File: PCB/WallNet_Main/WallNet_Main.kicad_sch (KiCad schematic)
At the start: 9 parts, among them J1 Conn_01x05_Pin, SW1 SW, U1 BT832

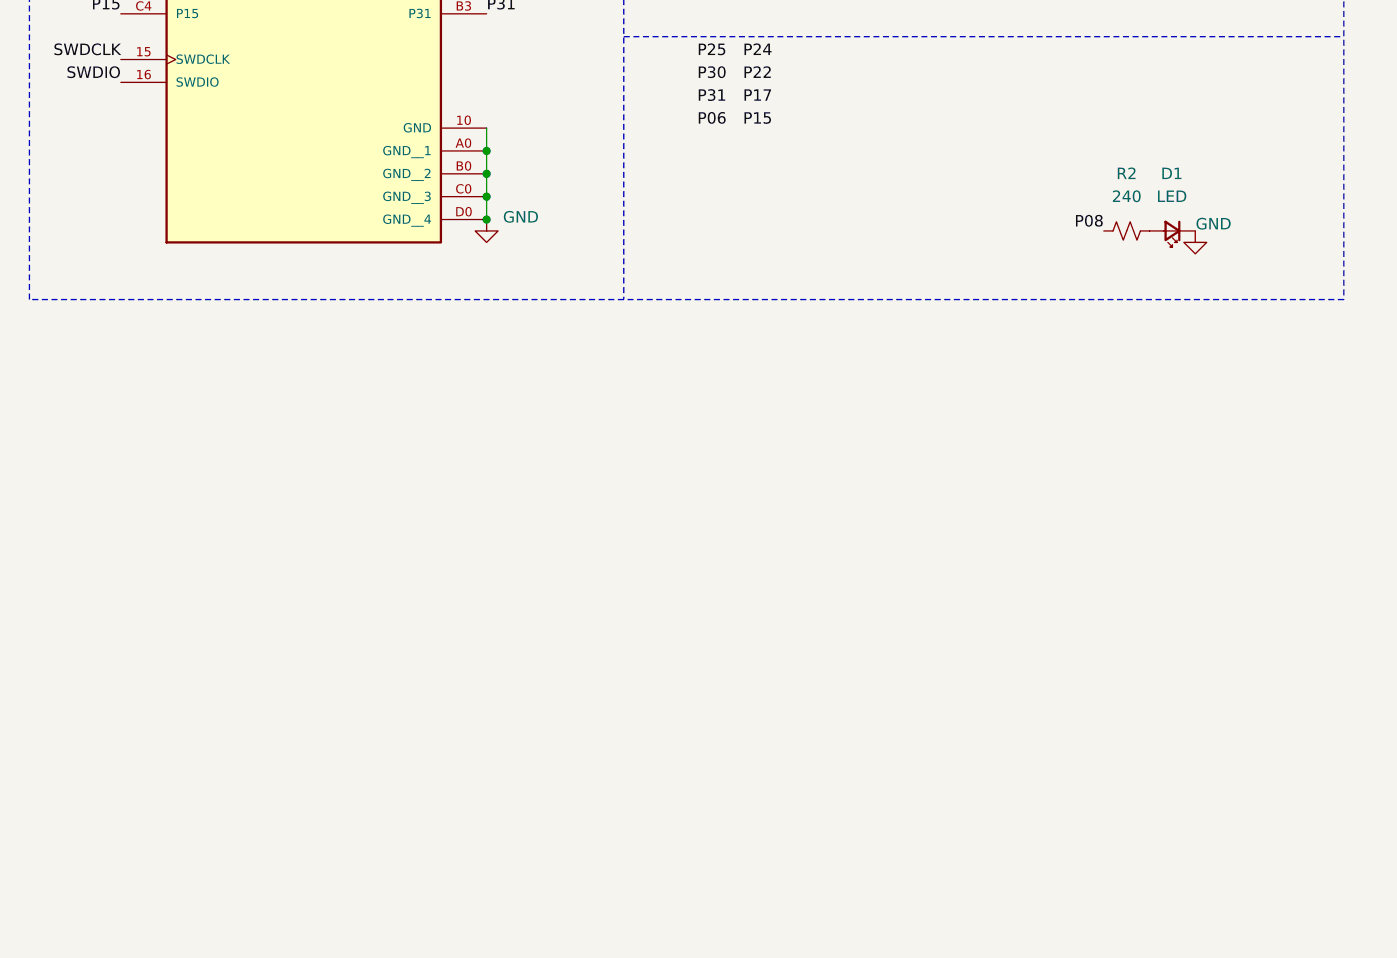
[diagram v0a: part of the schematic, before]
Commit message: "added test point debugging and mounting holes"
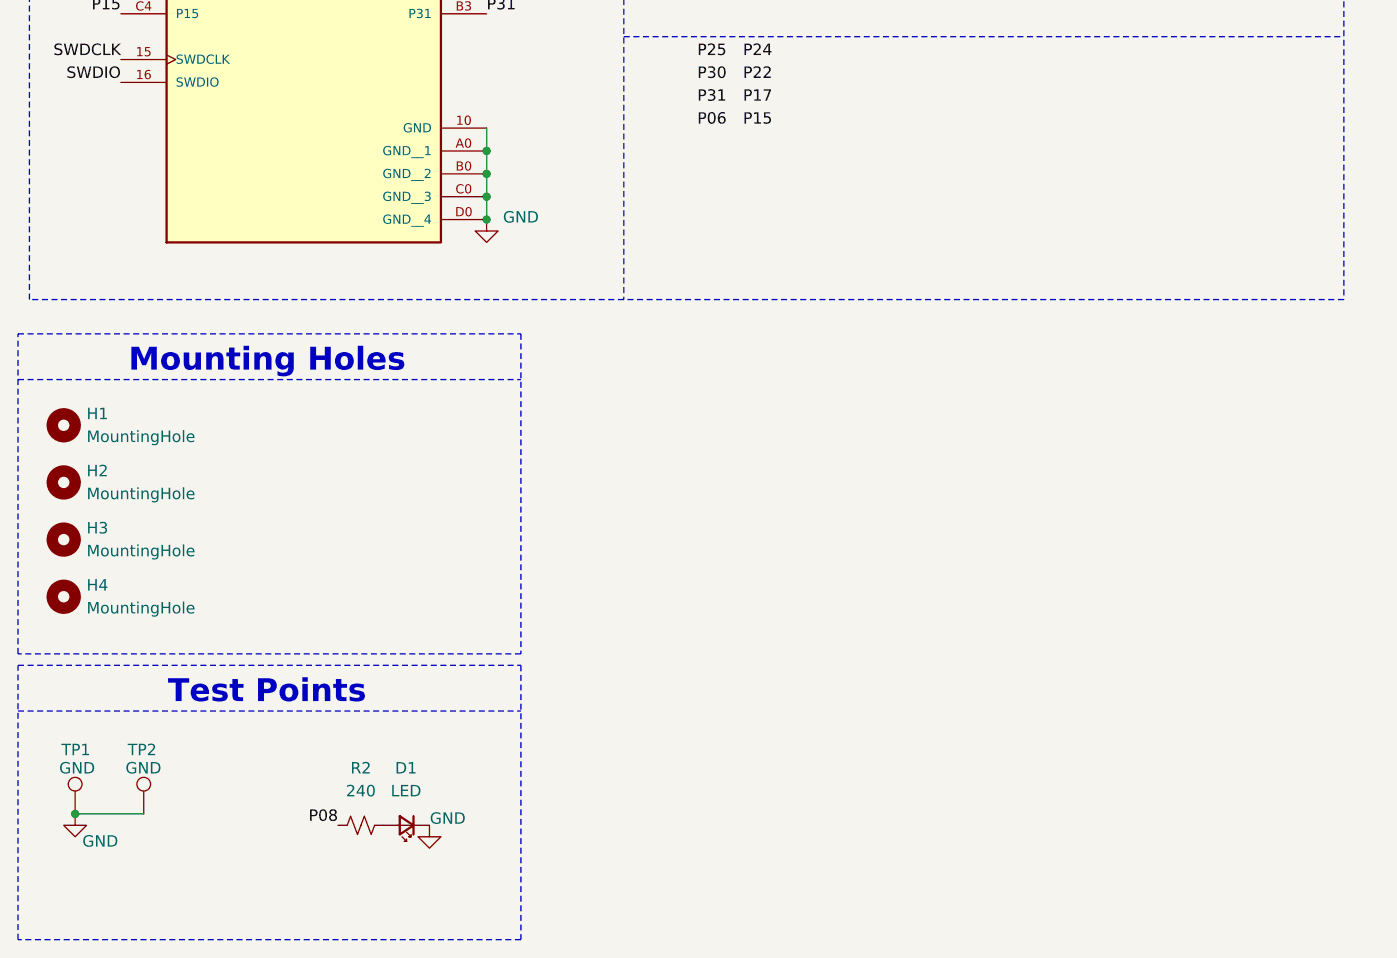
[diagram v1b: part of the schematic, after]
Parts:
- added H1, H2, H3, H4: MountingHole, MountingHole:MountingHole_4.3mm_M4, symbol Mechanical:MountingHole
- added TP1: GND, TestPoint:TestPoint_Pad_D1.0mm, symbol Connector:TestPoint
- added TP2: GND, 5001:KEYSTONE_5001, symbol Connector:TestPoint
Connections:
- net GND: now also TP1.1, TP2.1
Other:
- note added: "Mounting Holes"
- note added: "Test Points"
- moved on the sheet: D1, R2

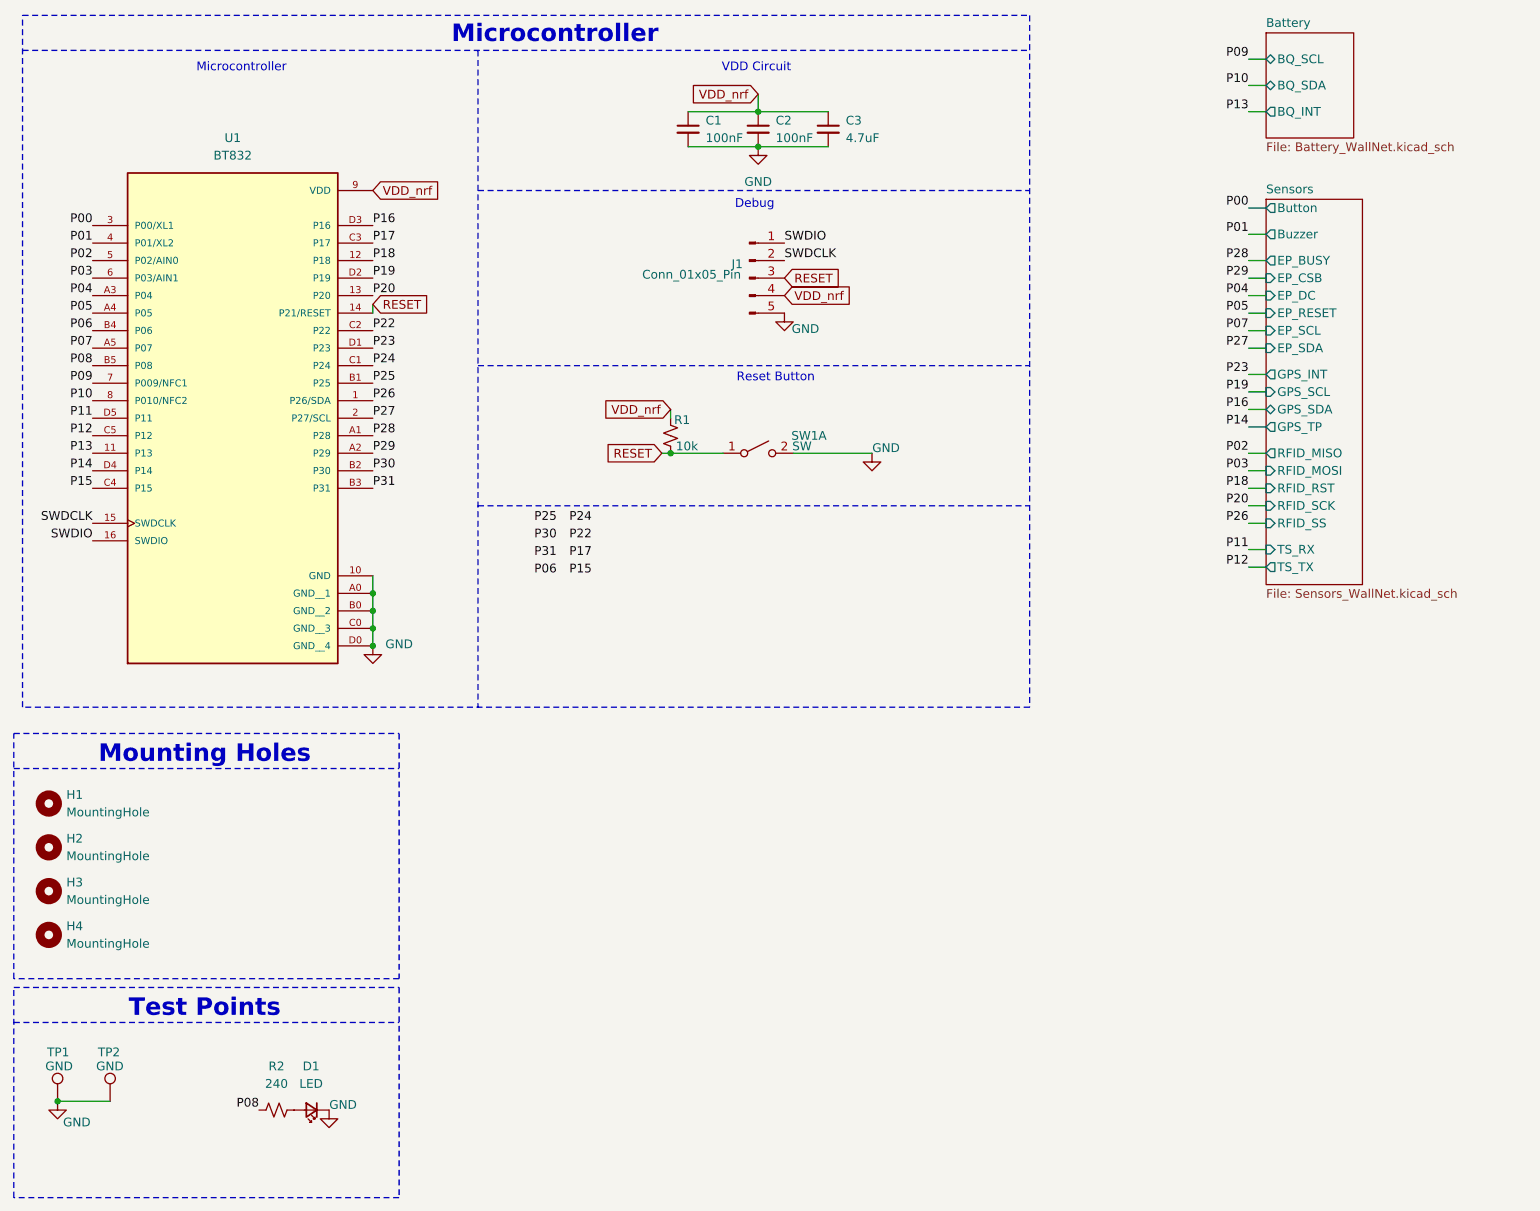
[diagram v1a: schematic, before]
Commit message: Finished adding cutout, via, and mount hole for RFID
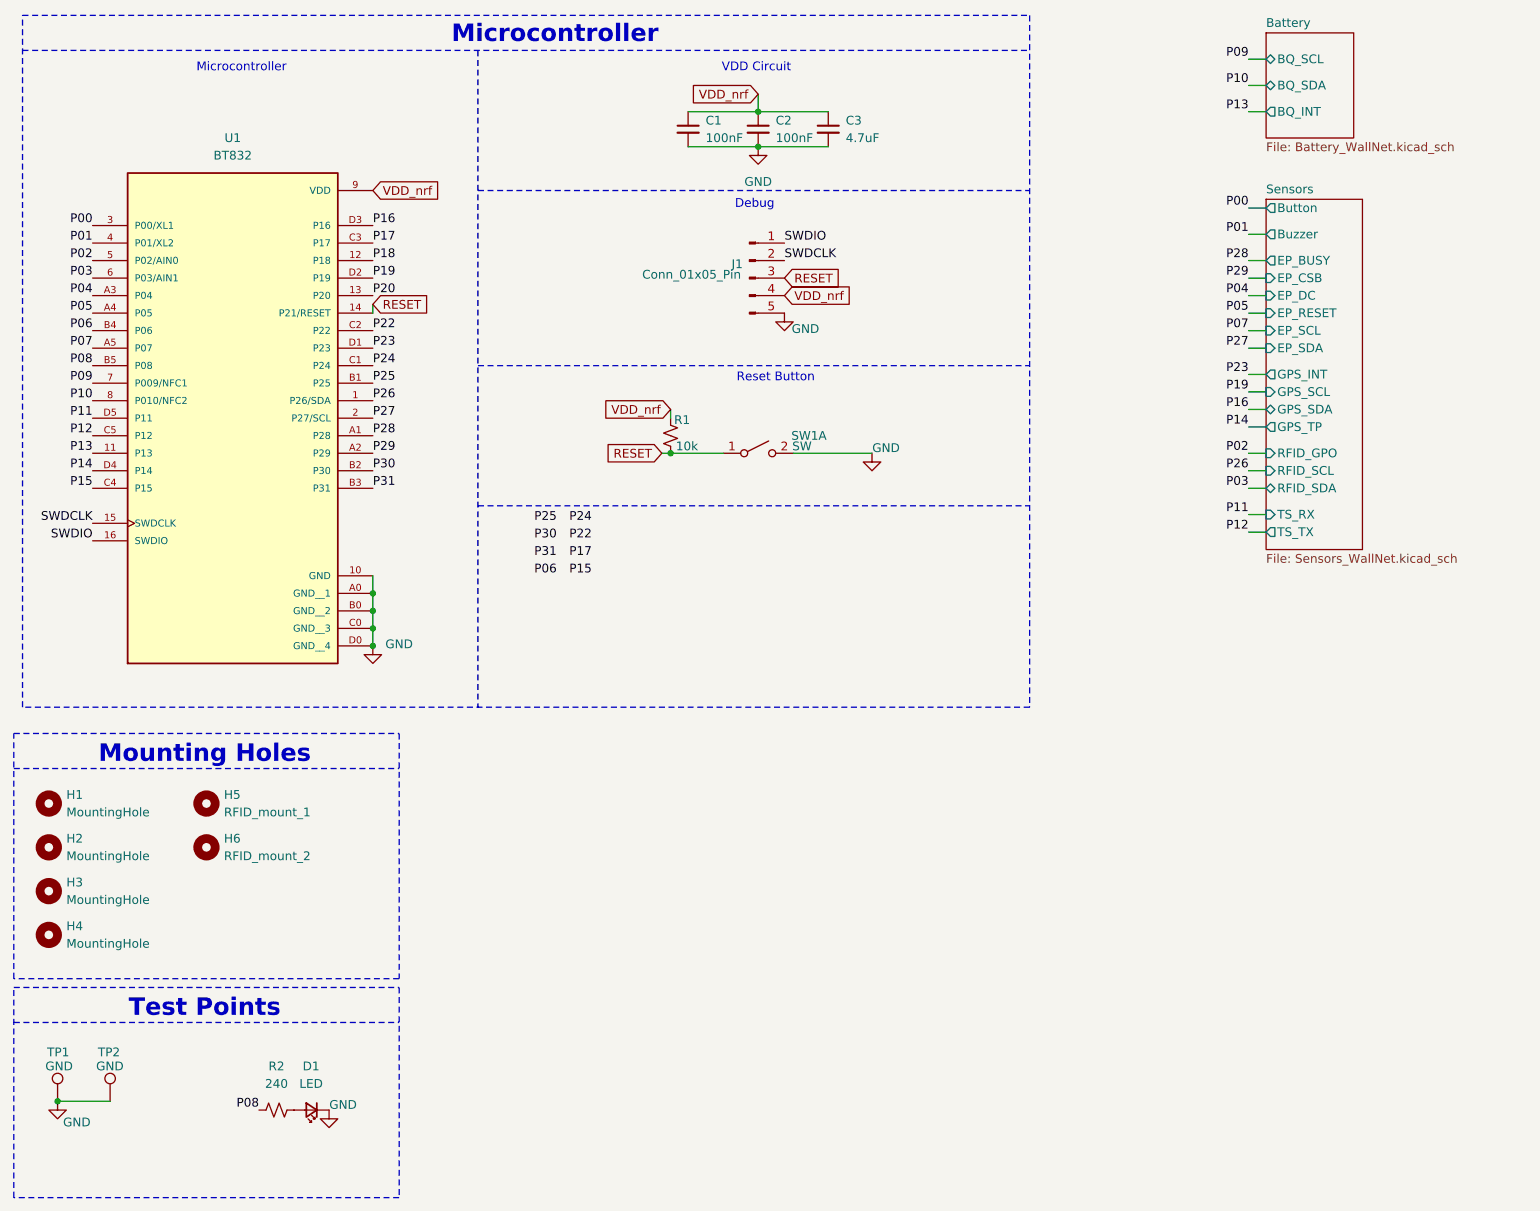
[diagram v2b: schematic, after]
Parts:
- added H5: RFID_mount_1, MountingHole:MountingHole_4.3mm_M4, symbol Mechanical:MountingHole
- added H6: RFID_mount_2, MountingHole:MountingHole_4.3mm_M4, symbol Mechanical:MountingHole
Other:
- sheet Sensors ports: added RFID_GPO, RFID_SCL, RFID_SDA; removed RFID_MISO, RFID_MOSI, RFID_RST, RFID_SCK, RFID_SS
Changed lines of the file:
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@@
 	(wire
 		(pts
-			(xy 68.58 64.77) (xy 68.58 66.04)
+			(xy 195.58 91.44) (xy 198.12 91.44)
 		)
 		(stroke
@@
 	(wire
 		(pts
-			(xy 111.76 86.36) (xy 119.38 86.36)
+			(xy 68.58 64.77) (xy 68.58 66.04)
 		)
 		(stroke
@@
 	(wire
 		(pts
-			(xy 195.58 50.8) (xy 198.12 50.8)
+			(xy 111.76 86.36) (xy 119.38 86.36)
 		)
 		(stroke
@@
 	(wire
 		(pts
-			(xy 195.58 102.87) (xy 198.12 102.87)
+			(xy 195.58 50.8) (xy 198.12 50.8)
 		)
 		(stroke
@@
 		)
 	)
-	(polyline
+	(wire
 		(pts
-			(xy 16.51 168.91) (xy 72.39 168.91)
+			(xy 195.58 88.9) (xy 198.12 88.9)
 		)
 		(stroke
 			(width 0)
-			(type dash)
+			(type default)
 		)
 	)
 	(wire
 		(pts
-			(xy 195.58 96.52) (xy 198.12 96.52)
+			(xy 195.58 97.79) (xy 198.12 97.79)
 		)
 		(stroke
@@
 		)
 	)
-	(wire
+	(polyline
 		(pts
-			(xy 195.58 91.44) (xy 198.12 91.44)
+			(xy 16.51 168.91) (xy 72.39 168.91)
 		)
 		(stroke
 			(width 0)
-			(type default)
+			(type dash)
 		)
 	)
@@
 		)
 	)
-	(wire
-		(pts
-			(xy 195.58 88.9) (xy 198.12 88.9)
-		)
-		(stroke
-			(width 0)
-			(type default)
-		)
-	)
 	(polyline
 		(pts
@@
 	(wire
 		(pts
-			(xy 195.58 100.33) (xy 198.12 100.33)
+			(xy 195.58 95.25) (xy 198.12 95.25)
 		)
 		(stroke
@@
 		)
 	)
-	(wire
-		(pts
-			(xy 195.58 86.36) (xy 198.12 86.36)
-		)
-		(stroke
-			(width 0)
-			(type default)
-		)
-	)
 	(polyline
 		(pts
@@
 	(wire
 		(pts
-			(xy 195.58 93.98) (xy 198.12 93.98)
+			(xy 195.58 66.04) (xy 198.12 66.04)
 		)
 		(stroke
@@
 		)
 	)
-	(wire
+	(polyline
 		(pts
-			(xy 195.58 66.04) (xy 198.12 66.04)
+			(xy 83.82 73.66) (xy 163.83 73.66)
 		)
 		(stroke
 			(width 0)
-			(type default)
+			(type dash)
 		)
 	)
-	(polyline
+	(wire
 		(pts
-			(xy 83.82 73.66) (xy 163.83 73.66)
+			(xy 195.58 86.36) (xy 198.12 86.36)
 		)
 		(stroke
 			(width 0)
-			(type dash)
+			(type default)
 		)
 	)
@@
 		)
 	)
-	(label "P20"
-		(at 195.58 93.98 180)
-		(effects
-			(font
-				(size 1.27 1.27)
-			)
-			(justify right bottom)
-		)
-	)
 	(label "P22"
 		(at 100.33 99.06 180)
@@
 		)
 	)
-	(label "P18"
-		(at 195.58 91.44 180)
-		(effects
-			(font
-				(size 1.27 1.27)
-			)
-			(justify right bottom)
-		)
-	)
 	(label "P12"
-		(at 195.58 102.87 180)
+		(at 195.58 97.79 180)
 		(effects
 			(font
@@
 	)
 	(label "P26"
-		(at 195.58 96.52 180)
+		(at 195.58 88.9 180)
 		(effects
 			(font
@@
 	)
 	(label "P11"
-		(at 195.58 100.33 180)
+		(at 195.58 95.25 180)
 		(effects
 			(font
@@
 		)
 	)
-	(label "P03"
-		(at 195.58 88.9 180)
-		(effects
-			(font
-				(size 1.27 1.27)
-			)
-			(justify right bottom)
-		)
-	)
 	(label "P04"
 		(at 27.94 63.5 180)
@@
 		)
 	)
+	(label "P03"
+		(at 195.58 91.44 180)
+		(effects
+			(font
+				(size 1.27 1.27)
+			)
+			(justify right bottom)
+		)
+	)
 	(label "P17"
 		(at 68.58 55.88 0)
@@
 	)
 	(symbol
+		(lib_id "Mechanical:MountingHole")
+		(at 44.45 143.51 0)
+		(unit 1)
+		(exclude_from_sim no)
+		(in_bom no)
+		(on_board yes)
+		(dnp no)
+		(fields_autoplaced yes)
+		(property "Reference" "H6"
+			(at 46.99 142.2399 0)
+			(effects
+				(font
+					(size 1.27 1.27)
+				)
+				(justify left)
+			)
+		)
+		(property "Value" "RFID_mount_2"
+			(at 46.99 144.7799 0)
+			(effects
+				(font
+					(size 1.27 1.27)
+				)
+				(justify left)
+			)
+		)
+		(property "Footprint" "MountingHole:MountingHole_4.3mm_M4"
+			(at 44.45 143.51 0)
+			(effects
+				(font
+					(size 1.27 1.27)
+				)
+				(hide yes)
+			)
+		)
+		(property "Datasheet" "~"
+			(at 44.45 143.51 0)
+			(effects
+				(font
+					(size 1.27 1.27)
+				)
+				(hide yes)
+			)
+		)
+		(property "Description" "Mounting Hole without connection"
+			(at 44.45 143.51 0)
+			(effects
+				(font
+					(size 1.27 1.27)
+				)
+				(hide yes)
+			)
+		)
+		(instances
+			(project "WallNet_Main"
+				(path "/3272dd14-9e34-4275-b10b-c06dab1b3ca1"
+					(reference "H6")
+					(unit 1)
+				)
+			)
+		)
+	)
+	(symbol
 		(lib_id "Switch:SW_DPST_x2")
 		(at 124.46 86.36 0)
@@
 	)
 	(symbol
+		(lib_id "Mechanical:MountingHole")
+		(at 44.45 137.16 0)
+		(unit 1)
+		(exclude_from_sim no)
+		(in_bom no)
+		(on_board yes)
+		(dnp no)
+		(fields_autoplaced yes)
+		(property "Reference" "H5"
+			(at 46.99 135.8899 0)
+			(effects
+				(font
+					(size 1.27 1.27)
+				)
+				(justify left)
+			)
+		)
+		(property "Value" "RFID_mount_1"
+			(at 46.99 138.4299 0)
+			(effects
+				(font
+					(size 1.27 1.27)
+				)
+				(justify left)
+			)
+		)
+		(property "Footprint" "MountingHole:MountingHole_4.3mm_M4"
+			(at 44.45 137.16 0)
+			(effects
+				(font
+					(size 1.27 1.27)
+				)
+				(hide yes)
+			)
+		)
+		(property "Datasheet" "~"
+			(at 44.45 137.16 0)
+			(effects
+				(font
+					(size 1.27 1.27)
+				)
+				(hide yes)
+			)
+		)
+		(property "Description" "Mounting Hole without connection"
+			(at 44.45 137.16 0)
+			(effects
+				(font
+					(size 1.27 1.27)
+				)
+				(hide yes)
+			)
+		)
+		(instances
+			(project "WallNet_Main"
+				(path "/3272dd14-9e34-4275-b10b-c06dab1b3ca1"
+					(reference "H5")
+					(unit 1)
+				)
+			)
+		)
+	)
+	(symbol
 		(lib_id "Device:R_Small_US")
 		(at 54.61 181.61 90)
@@
 	(sheet
 		(at 198.12 49.53)
-		(size 13.97 55.88)
+		(size 13.97 50.8)
 		(exclude_from_sim no)
 		(in_bom yes)
@@
 		)
 		(property "Sheetfile" "Sensors_WallNet.kicad_sch"
-			(at 198.12 105.9946 0)
+			(at 198.12 100.9146 0)
 			(effects
 				(font
@@
 			)
 		)
-		(pin "RFID_MISO" output
-			(at 198.12 86.36 180)
-			(effects
-				(font
-					(size 1.27 1.27)
-				)
-				(justify left)
-			)
-		)
-		(pin "RFID_MOSI" input
-			(at 198.12 88.9 180)
-			(effects
-				(font
-					(size 1.27 1.27)
-				)
-				(justify left)
-			)
-		)
-		(pin "RFID_RST" input
-			(at 198.12 91.44 180)
+		(pin "TS_RX" input
+			(at 198.12 95.25 180)
 			(effects
 				(font
@@
 			)
 		)
-		(pin "RFID_SCK" input
-			(at 198.12 93.98 180)
+		(pin "TS_TX" output
+			(at 198.12 97.79 180)
 			(effects
 				(font
@@
 			)
 		)
-		(pin "RFID_SS" input
-			(at 198.12 96.52 180)
+		(pin "RFID_GPO" input
+			(at 198.12 86.36 180)
 			(effects
 				(font
@@
 			)
 		)
-		(pin "TS_RX" input
-			(at 198.12 100.33 180)
+		(pin "RFID_SCL" input
+			(at 198.12 88.9 180)
 			(effects
 				(font
@@
 			)
 		)
-		(pin "TS_TX" output
-			(at 198.12 102.87 180)
+		(pin "RFID_SDA" bidirectional
+			(at 198.12 91.44 180)
 			(effects
 				(font
